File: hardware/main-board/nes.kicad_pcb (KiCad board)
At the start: 2 copper layers, 127 x 114.3 mm, 138 parts, among them J1 Power Jack, J2 Input Board, J3 Speaker, J4 Program, J5 NHD OLED Connector, J6 microSD Socket, Q1 S8050, Q2 S8050, Q3 S8050, SW1 NES Reset, SW2 ESP Reset, U1 R-78E5.0-0.5, U10 74HCT00, U11 PCA9564, U12 MCP7940N, U13 ESP-WROOM-32, U14 TSL251R, U15 EClamp2410P, U2 R-78E3.3-0.5, U3 74LVC1404, U4 RP2A03, U5 74HCT138, U6 LM4889, U7 AS6C6264, U8 MCP40D17, U9 AT28C64B, Y1 21.5 MHz, Y2 32.768 kHz

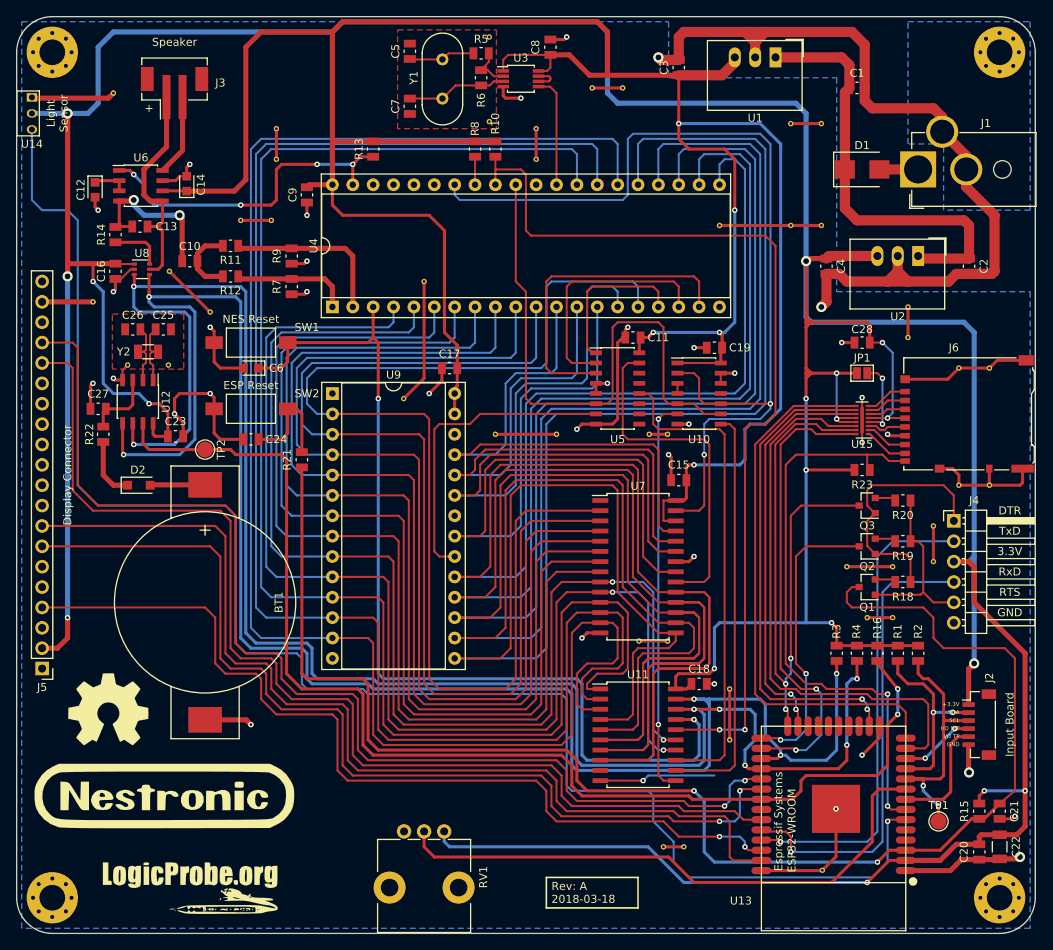
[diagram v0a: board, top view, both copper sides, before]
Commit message: Remove the ambient light sensor from the main board
Fixes #9
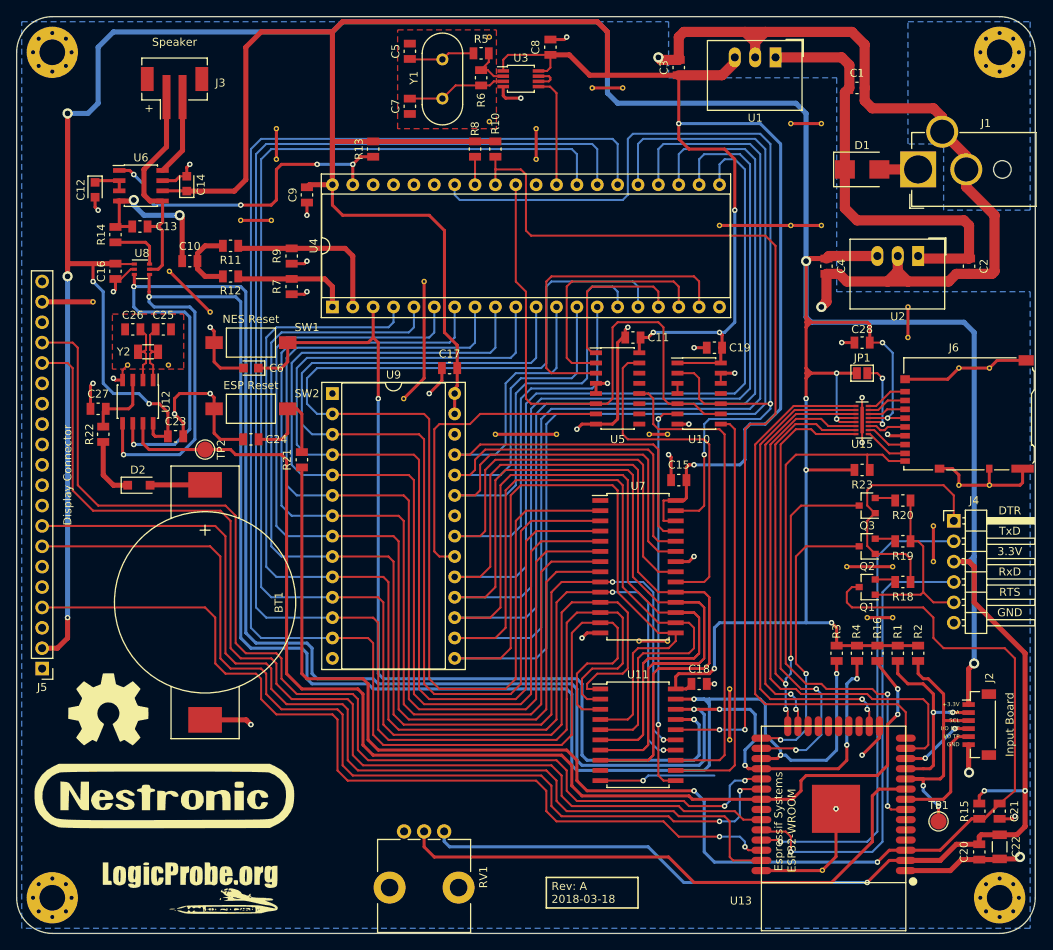
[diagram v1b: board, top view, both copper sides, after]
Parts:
- removed the REF** at (140.3, 136.5)
- removed the REF** at (142.9, 136.5)
- removed U14: TSL251R, lib_fp:S-3
- moved REF** 14.6 mm to (57.1, 41.9)
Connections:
- U13 pad 6: /ESP32 Microcontroller/LUM -> Net-(U13-Pad6)
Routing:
- net /ESP32 Microcontroller/LUM: track 199.0 -> 0.00 mm, vias 1 -> 0
- net GND: track 416.5 -> 403.5 mm
- net +3V3: track 620.1 -> 615.6 mm
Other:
- board text removed: "Light Sensor"

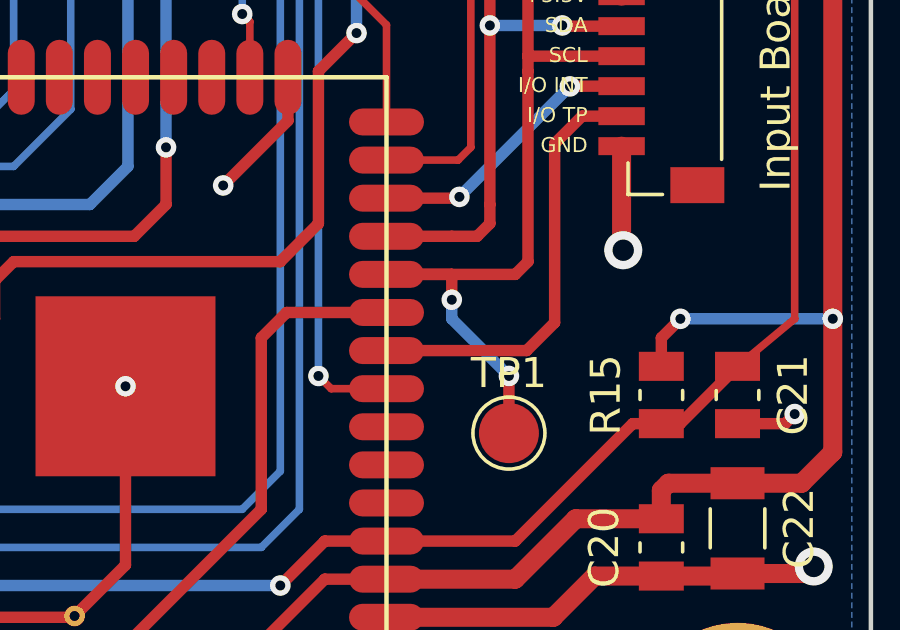
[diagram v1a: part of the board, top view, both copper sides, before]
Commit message: Move TP1 over to GPIO27
This moves the ADC calibration test point from a pin that always has a
pull-up resistor, to one that only has issues if the input board is
plugged in.

Fixes #6
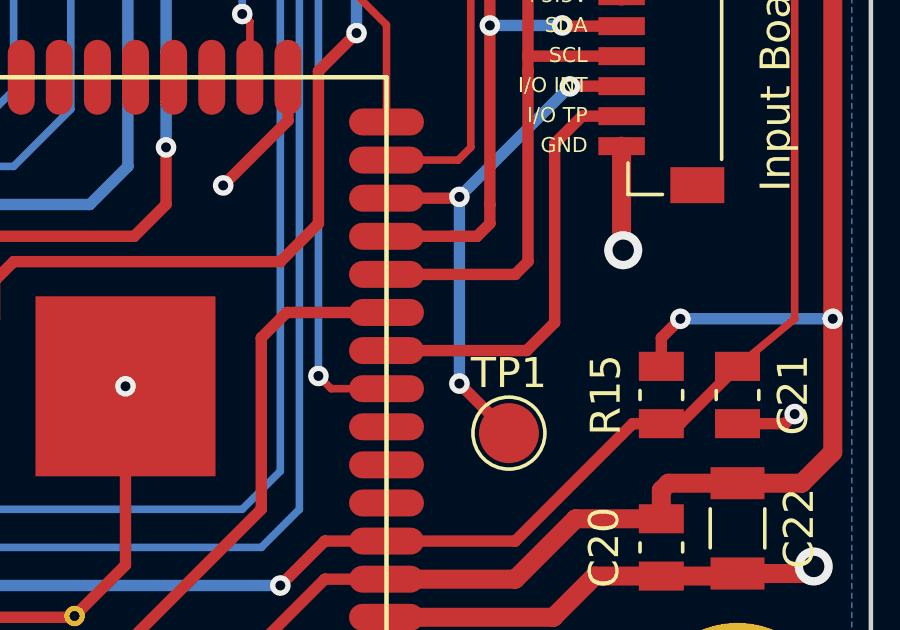
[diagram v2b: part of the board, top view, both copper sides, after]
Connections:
- TP1 pad 1: /ESP32 Microcontroller/SCL1 -> /ESP32 Microcontroller/I/O_INT
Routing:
- net /ESP32 Microcontroller/I/O_INT: track 9.38 -> 17.9 mm, vias 2 -> 3
- net /ESP32 Microcontroller/SCL1: track 32.2 -> 24.0 mm, vias 2 -> 0
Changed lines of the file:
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@@
     (thickness 1.6002)
     (drawings 46)
-    (tracks 1741)
+    (tracks 1737)
     (zones 0)
     (modules 135)
@@
   )
   (setup
-    (last_trace_width 0.1524)
+    (last_trace_width 0.381)
     (user_trace_width 0.254)
     (user_trace_width 0.381)
@@
     (fp_circle (center 0 0) (end 0 1.2) (layer F.SilkS) (width 0.12))
     (pad 1 smd circle (at 0 0) (size 2 2) (layers F.Cu F.Mask)
-      (net 21 "/ESP32 Microcontroller/SCL1"))
+      (net 22 "/ESP32 Microcontroller/I/O_INT"))
   )
   (module TestPoint:TestPoint_Pad_D2.0mm (layer F.Cu)
@@
   (segment (start 175.26 127.635) (end 175.26 121.285) (width 0.381) (layer F.Cu) (net 21))
   (segment (start 174.836 128.059) (end 175.26 127.635) (width 0.381) (layer F.Cu) (net 21))
-  (segment (start 174.625 133.35) (end 174.625 131.445) (width 0.381) (layer F.Cu) (net 21))
-  (segment (start 172.72 128.059) (end 170.544 128.059) (width 0.381) (layer F.Cu) (net 21))
-  (segment (start 172.72 128.905) (end 172.72 128.059) (width 0.381) (layer F.Cu) (net 21))
-  (via (at 172.72 128.905) (size 0.6858) (drill 0.3302) (layers F.Cu B.Cu) (net 21))
-  (segment (start 172.72 129.54) (end 172.72 128.905) (width 0.381) (layer B.Cu) (net 21))
-  (segment (start 174.625 131.445) (end 172.72 129.54) (width 0.381) (layer B.Cu) (net 21))
-  (via (at 174.625 131.445) (size 0.6858) (drill 0.3302) (layers F.Cu B.Cu) (net 21))
+  (segment (start 174.625 133.35) (end 172.974 131.699) (width 0.381) (layer F.Cu) (net 22))
+  (segment (start 172.974 131.699) (end 172.974 125.476) (width 0.381) (layer B.Cu) (net 22))
+  (via (at 172.974 131.699) (size 0.6858) (drill 0.3302) (layers F.Cu B.Cu) (net 22))
   (segment (start 170.544 125.519) (end 172.931 125.519) (width 0.381) (layer F.Cu) (net 22))
   (segment (start 176.665 121.785) (end 178.38 121.785) (width 0.381) (layer F.Cu) (net 22))

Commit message: Change amplifier gain resistor from 20k to 4.7k
In testing, the minimum volume with 10k was still a little bit too loud,
so going with 4.7k for now. This is easily adjustible in the future
without any actual board layout changes.

Fixes #4
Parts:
- R14: value 20k -> 4.7k
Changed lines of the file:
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@@
   )
   (setup
-    (last_trace_width 0.381)
+    (last_trace_width 0.1524)
     (user_trace_width 0.254)
     (user_trace_width 0.381)
@@
       (effects (font (size 1 1) (thickness 0.15)))
     )
-    (fp_text value 20k (at 2.54 2.794 270) (layer F.Fab)
-      (effects (font (size 1 1) (thickness 0.15)))
-    )
+    (fp_text value 4.7k (at 2.54 2.794 270) (layer F.Fab)
+      (effects (font (size 1 1) (thickness 0.15)))
+    )

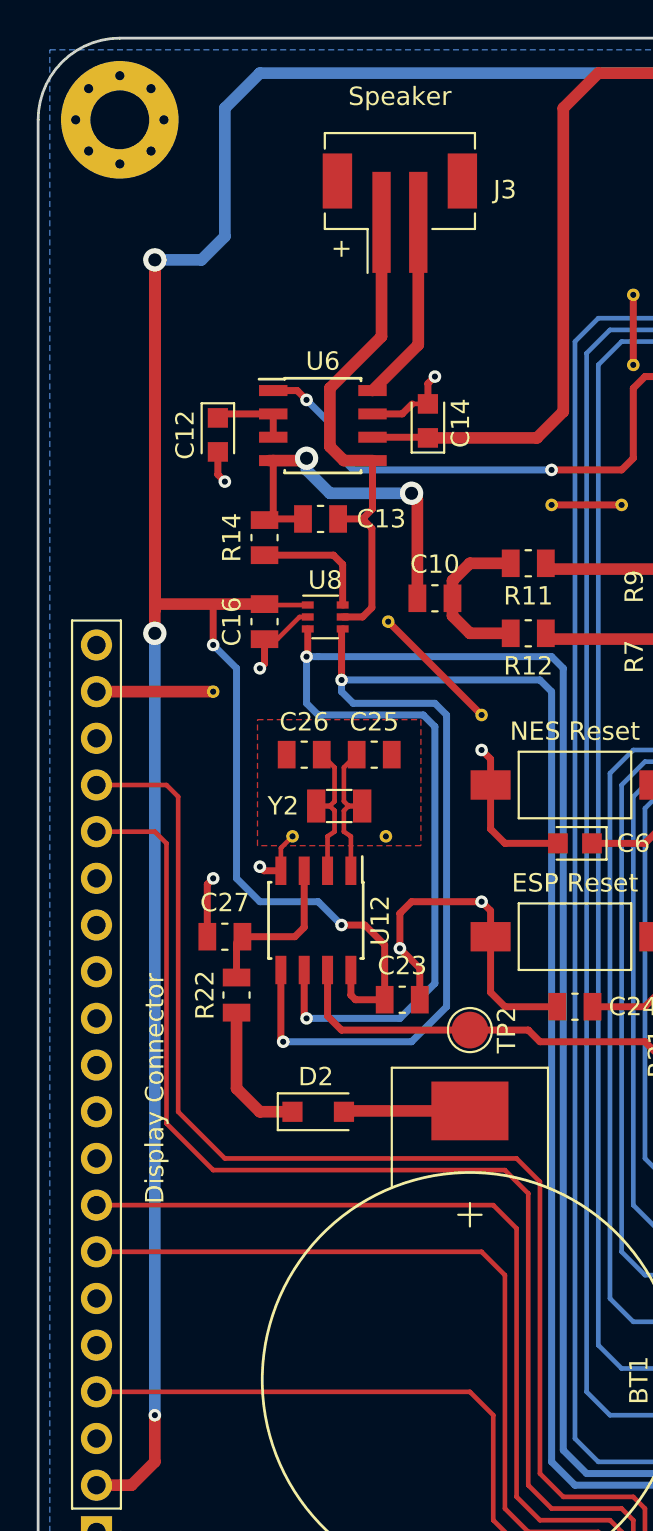
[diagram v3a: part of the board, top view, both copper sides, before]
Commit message: Changed U8 Vdd from 3.3V to 5V
Had to reroute a few other traces in the process of doing this, and was
able to remove some vias from a 3.3V line. Also added some stitching
vias to re-connect the ground plane that changed as a result.
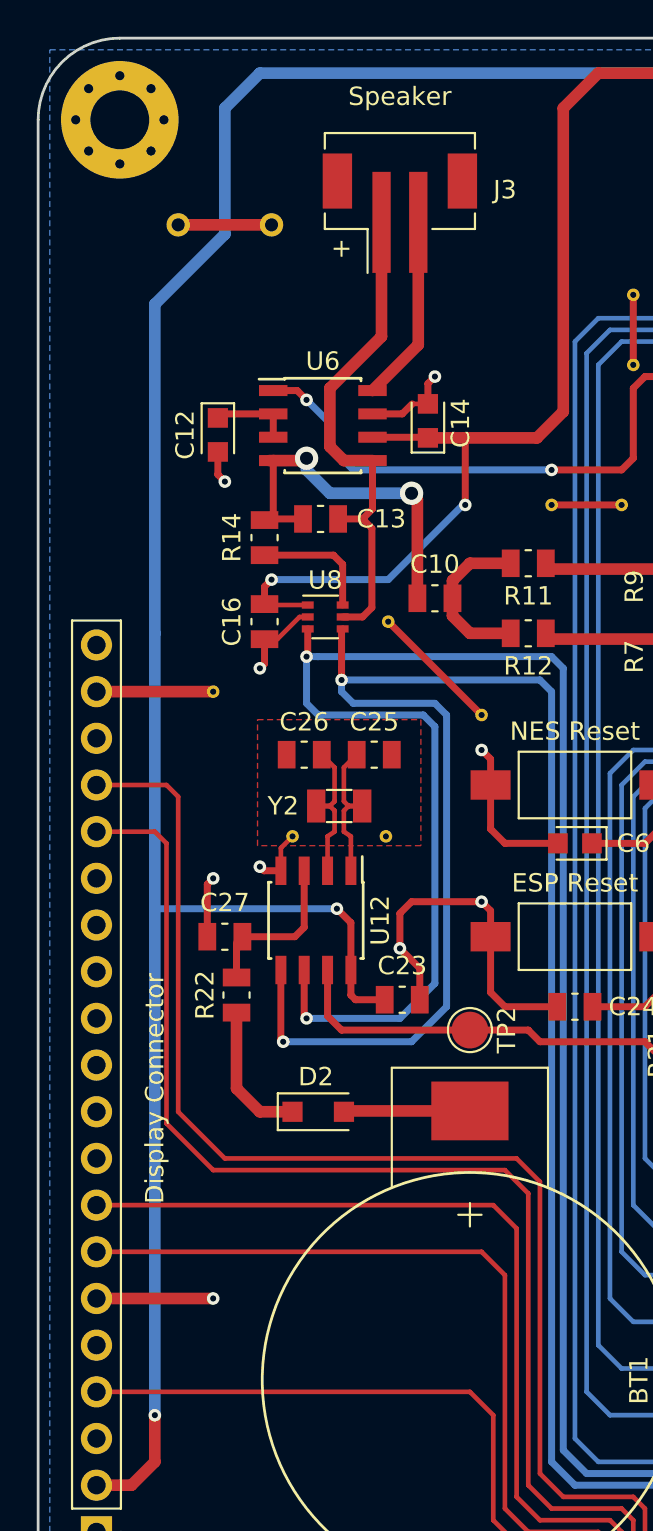
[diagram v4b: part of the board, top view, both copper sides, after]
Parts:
- added REF**: Via_50mill, lib_fp:Via_50mill, F.Cu at (67.3, 43.2)
- added REF**: Via_50mill, lib_fp:Via_50mill, F.Cu at (72.4, 43.2)
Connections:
- C16 pad 1: +3V3 -> +5V
- U8 pad 1: +3V3 -> +5V
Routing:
- net +3V3: track 615.6 -> 569.4 mm, vias 18 -> 15
- net +5V: track 340.7 -> 360.6 mm, vias 5 -> 7
- net GND: track 403.5 -> 414.9 mm, vias 37 -> 38

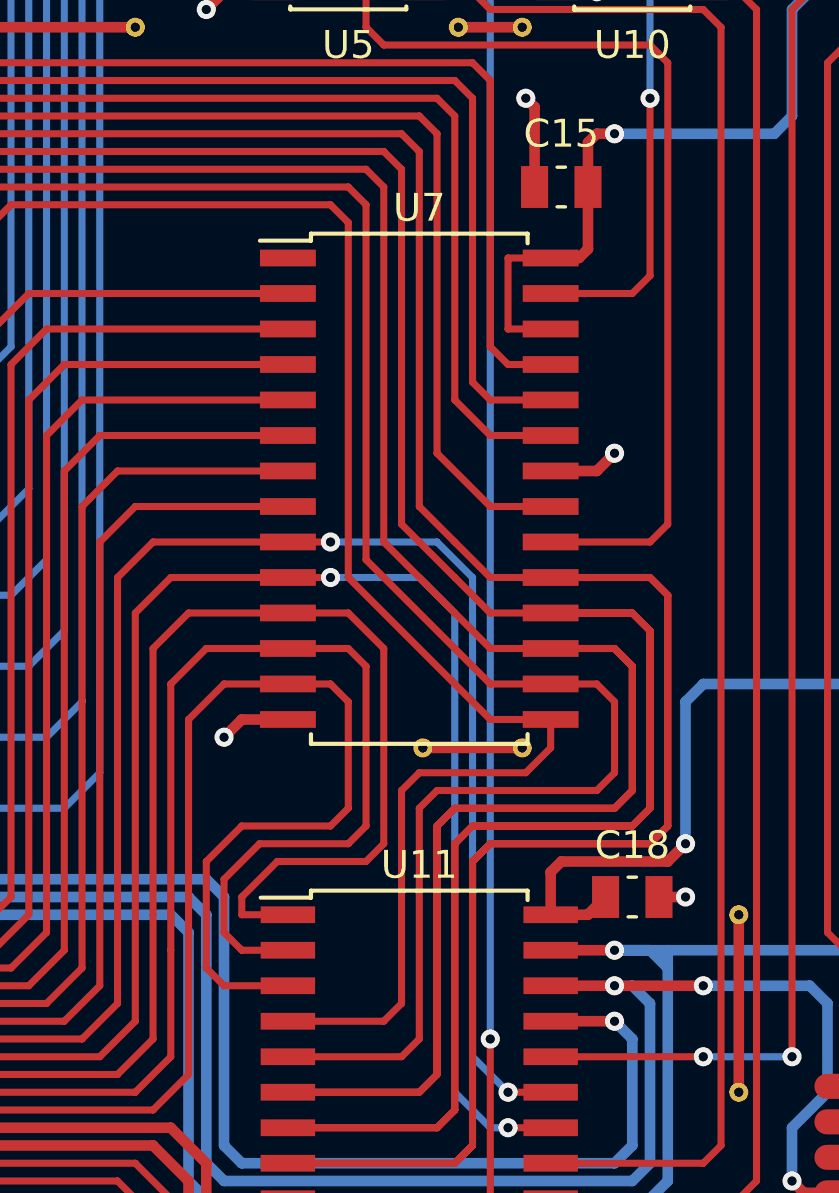
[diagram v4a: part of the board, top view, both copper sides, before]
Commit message: Change U7 footprint to one that more closely matches the component
This involved adding a custom SOIC-28 footprint variant for the
AS6C6264.

This IC uses what it calls a "28-pin 330 mil SOP" package, which is not
in the standard libraries. Its closest match is KiCad's SOIC-28W, but it
is slightly wider and taller. This footprint and 3D model is based on
using the IC's datasheet and the reference datasheets from KiCad's
footprint and 3D model to determine small adjustments.

The replacement footprint is slightly wider, so some routing was
adjusted. However, it is mostly a drop-in replacement.

Fixes #1
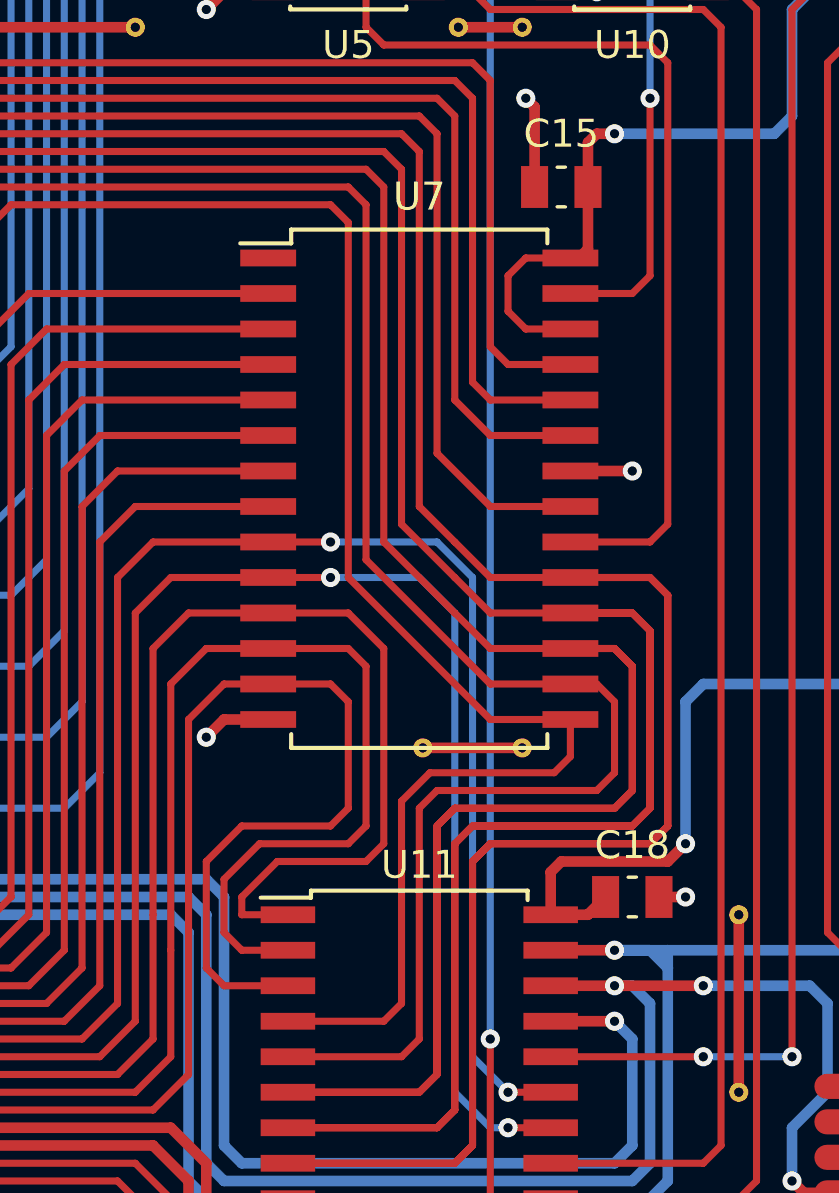
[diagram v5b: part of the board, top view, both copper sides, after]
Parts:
- U7: footprint Package_SO:SOIC-28W_7.5x17.9mm_P1.27mm -> lib_fp:SOIC-28W_8.636x18.491mm_P1.27mm
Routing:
- net +5V: track 360.6 -> 361.3 mm
- net /NES CPU/D3: track 203.4 -> 204.1 mm
